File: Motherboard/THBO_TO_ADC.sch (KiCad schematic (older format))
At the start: 22 parts, among them P1201 CONN_02X08, U1201 ADS7953_38TSSOP, U1202 OPA192, U1204 REF5025_TI

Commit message: computer is dying
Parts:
- added R1207: 0, Resistors_SMD:R_0805_HandSoldering, symbol R
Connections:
- net at R1205.2, U1202.1 (Vout): now also R1207.1; no longer U1202.4 (-)
- new net: R1207.2, U1202.4 (-)

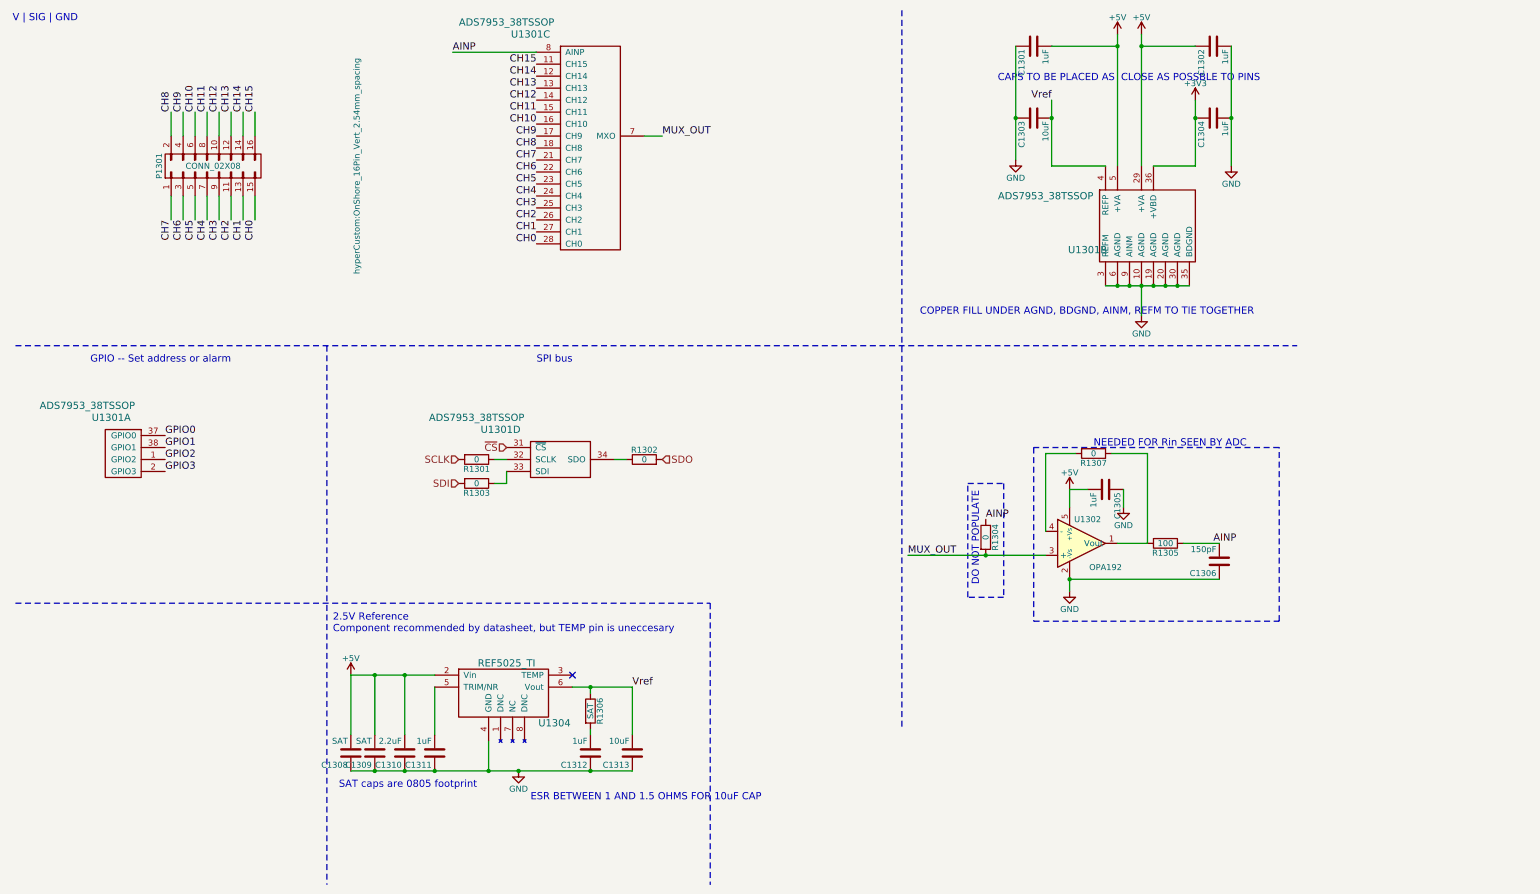
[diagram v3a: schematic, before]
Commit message: Mobo Version 2.1 Added Silk scren Ground Plane Cleanup Pinout changes on Beaglebone Headers, need to modify cabeling from V2.0 and earlier Added power sequencing for ADCs Removed Y3 ADC Removed TI Battery Board I2C lines More 5V connectors on Board Adjusted ADC Connecter pinout to match interface modules
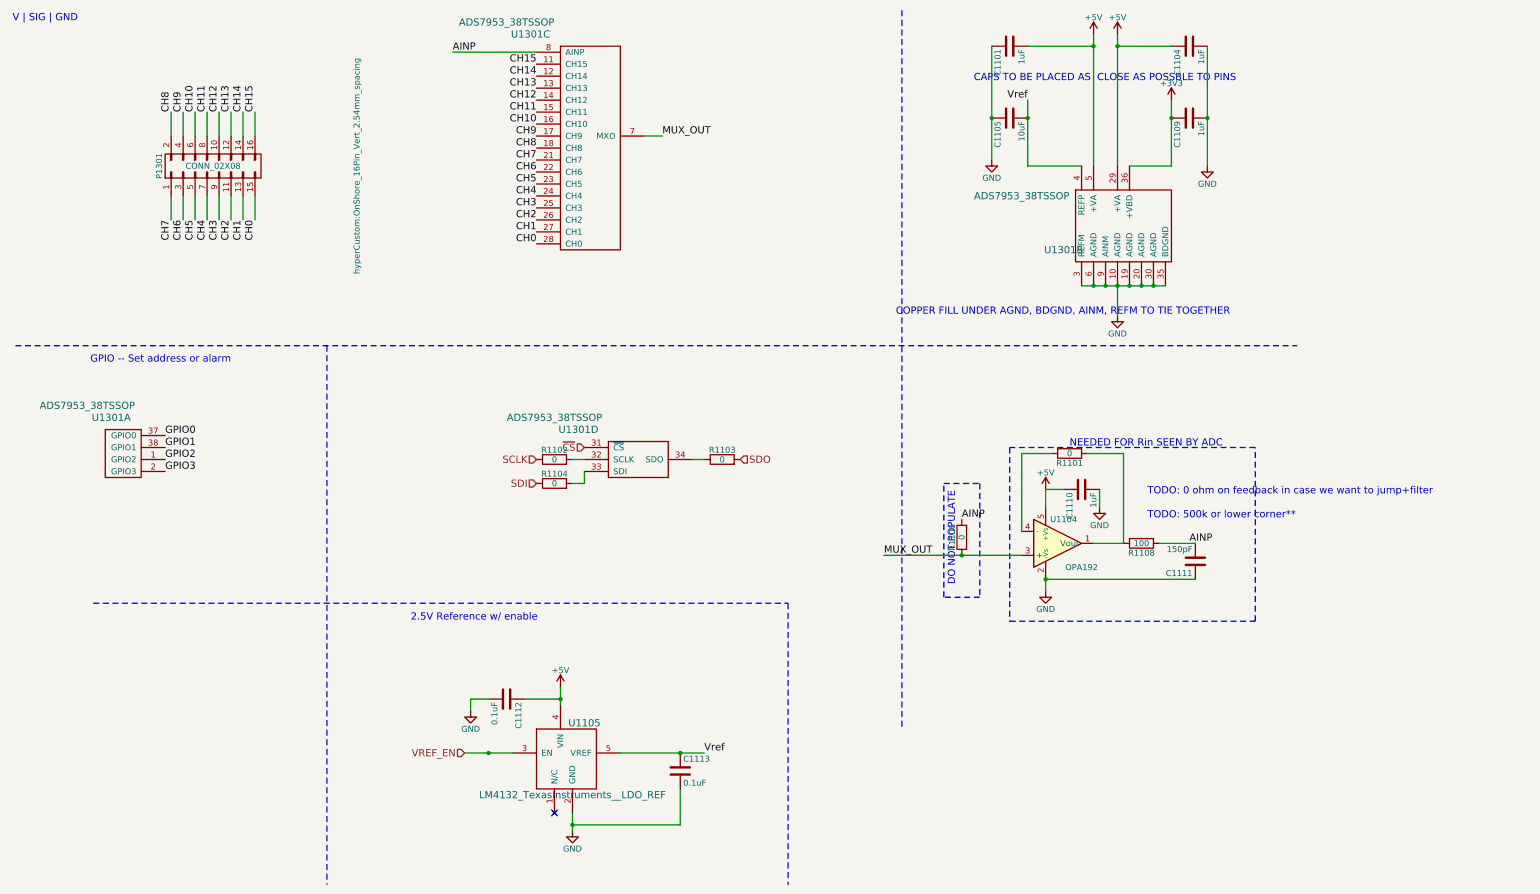
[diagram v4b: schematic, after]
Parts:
- removed C1201, C1202, C1204, C1205, C1211, C1212: 1uF, Capacitors_SMD:C_0603_HandSoldering, symbol C
- removed C1203, C1213: 10uF, Capacitors_SMD:C_0603_HandSoldering, symbol C
- removed C1206: 150pF, Capacitors_SMD:C_0603_HandSoldering, symbol C
- removed C1208, C1209: SAT, Capacitors_SMD:C_0805_HandSoldering, symbol C
- removed C1210: 2.2uF, Capacitors_SMD:C_0603_HandSoldering, symbol C
- removed R1201, R1202, R1203, R1204, R1207: 0, Resistors_SMD:R_0805_HandSoldering, symbol R
- removed R1205: 100, Resistors_SMD:R_0603_HandSoldering, symbol R
- removed R1206: SAT, Resistors_SMD:R_0805_HandSoldering, symbol R
- removed unit 2 of U1201
- removed U1202: OPA192, TO_SOT_Packages_SMD:SOT-23-5_HandSoldering, symbol OPA656
- removed U1204: REF5025_TI, Housings_SSOP:TSSOP-8_3x3mm_Pitch0.65mm, symbol REF2025_TI
- added C1001, C1002, C1004, C1005: 1uF, Capacitors_SMD:C_0603_HandSoldering, symbol C
- added C1003: 10uF, Capacitors_SMD:C_0603_HandSoldering, symbol C
- added C1006: 150pF, Capacitors_SMD:C_0603_HandSoldering, symbol C
- added C1007, C1008: 0.1uF, Capacitors_SMD:C_0805_HandSoldering, symbol C
- added R1005, R1006, R1007, R1008, R1009: 0, Resistors_SMD:R_0805_HandSoldering, symbol R
- added R1010: 100, Resistors_SMD:R_0603_HandSoldering, symbol R
- added U1001: OPA192, TO_SOT_Packages_SMD:SOT-23-5_HandSoldering, symbol OPA656
- added U1002: LM4132_TexasInstruments__LDO_REF, TO_SOT_Packages_SMD:SOT-23-5_HandSoldering, symbol LM4132_TexasInstruments__LDO_REF
- added U1301: ADS7953_38TSSOP, moboFootprints:TSSOP-38_4.4x9.7mm_Pitch0.5mm, symbol ADS7953_38TSSOP
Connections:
- net +3V3: now also C1004.1, U1301.36 (+VBD)
- net +5V: now also C1001.2, C1002.1, C1005.1, C1007.1, U1001.5 (+Vs), U1002.4 (VIN), U1301.29 (+VA), U1301.5 (+VA)
- net AINP: now also C1006.2, R1009.2, R1010.1
- net GND: now also C1001.1, C1002.2, C1003.1, C1004.2, C1005.2, C1006.1, C1007.2, C1008.2, U1001.2 (-Vs), U1002.2 (GND), U1301.10 (AGND), U1301.19 (AGND), U1301.20 (AGND), U1301.3 (REFM), U1301.30 (AGND), U1301.35 (BDGND), U1301.6 (AGND), U1301.9 (AINM)
- net MUX_OUT: now also R1009.1, U1001.3 (+)
- net SCLK: now also R1006.1
- net SDI: now also R1008.1
- net SDO: now also R1007.2
- net Vref: now also C1003.2, C1008.1, U1002.5 (VREF), U1301.4 (REFP)
- net at U1201.32 (SCLK): now also R1006.2
- net at U1201.33 (SDI): now also R1008.2
- net at U1201.34 (SDO): now also R1007.1
- new net: R1005.1, R1010.2, U1001.1 (Vout)
- new net: R1005.2, U1001.4 (-)
- new net VREF_EN: U1002.3 (EN)
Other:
- note added: "2.5V Reference w/ enable\n\n"
- note added: "TODO: 0 ohm on feedback in case we want to jump+filter"
- note added: "TODO: 500k or lower corner**"
- note removed: "2.5V Reference\nComponent recommended by datasheet, but TEMP pin is uneccesary\n"
- note removed: "ESR BETWEEN 1 AND 1.5 OHMS FOR 10uF CAP\n\n"
- note removed: "SAT caps are 0805 footprint\n"
- note removed: "SPI bus"
